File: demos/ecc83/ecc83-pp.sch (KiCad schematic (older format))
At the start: 15 parts, among them P1 IN, P2 OUT, P3 POWER, P4 CONN_2, P5 CONN_1, P6 CONN_1, P7 CONN_1, P8 CONN_1, U1 ECC83

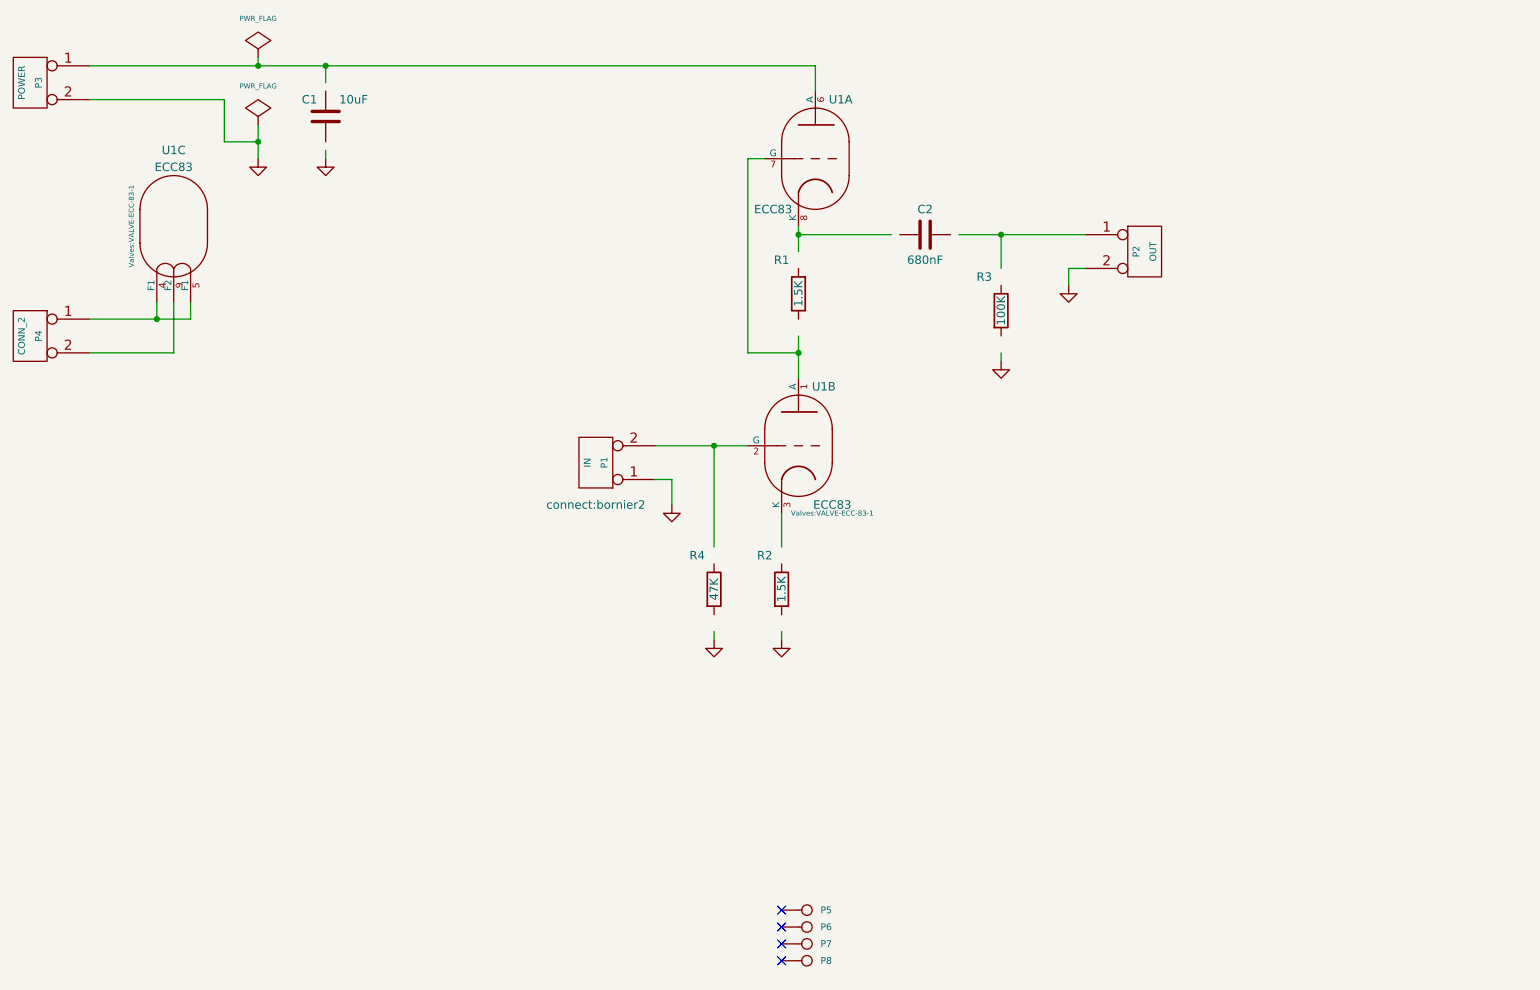
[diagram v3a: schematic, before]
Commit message: Demos: make a private library for each demo, to avoid issues when using modified kicad new schematic libraries
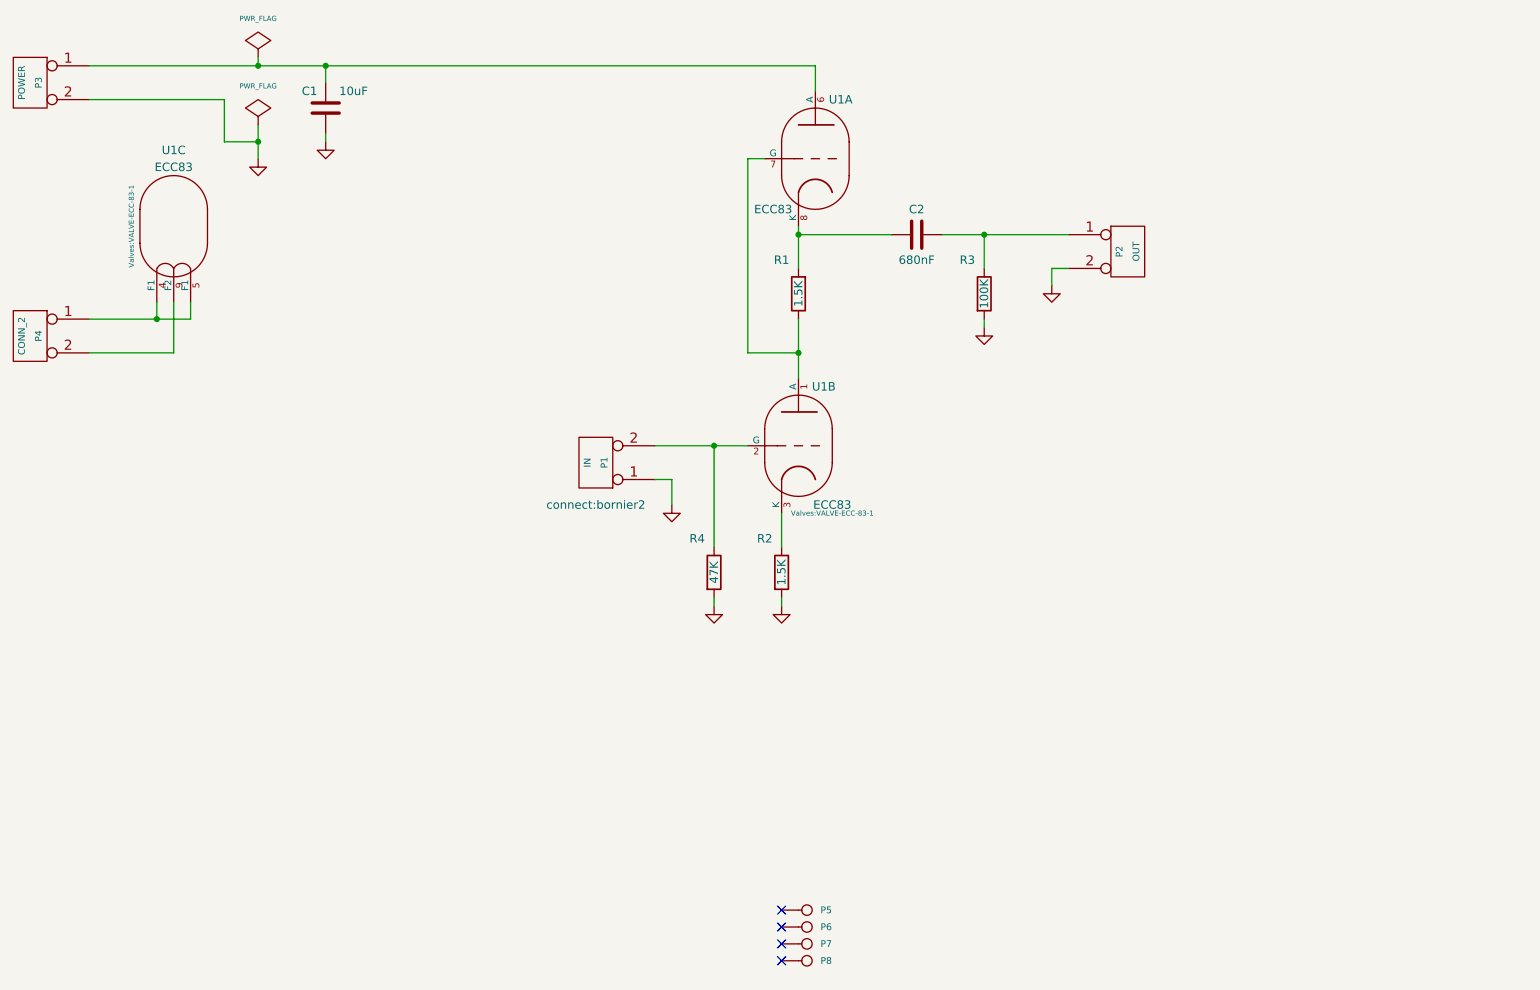
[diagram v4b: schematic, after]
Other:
- moved on the sheet: C1, C2, P2, R2, R3, R4
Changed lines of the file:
@@
 EESchema Schematic File Version 2
-LIBS:power
-LIBS:device
-LIBS:conn
-LIBS:valves
-LIBS:linear
-LIBS:regul
-LIBS:special
-LIBS:ecc83-pp-cache
+LIBS:ecc83_schlib
 EELAYER 25 0
 EELAYER END
@@
 Connection ~ 3400 2000
 Wire Wire Line
-	7150 3000 7900 3000
-Wire Wire Line
-	7400 3000 7400 3200
+	7050 3000 7800 3000
+Wire Wire Line
+	7300 3000 7300 3200
 Wire Wire Line
 	2000 3500 2600 3500
@@
 	2400 3500 2400 3400
 Wire Wire Line
-	6200 3600 6200 3850
+	6200 3500 6200 3850
 $Comp
 L ECC83 U1
@@
 L GND #PWR01
 U 1 1 457DBAF8
-P 7800 3300
-F 0 "#PWR01" H 7800 3300 30  0001 C CNN
-F 1 "GND" H 7800 3230 30  0001 C CNN
-F 2 "" H 7800 3300 60  0001 C CNN
-F 3 "" H 7800 3300 60  0001 C CNN
-	1    7800 3300
+P 7700 3300
+F 0 "#PWR01" H 7700 3300 30  0001 C CNN
+F 1 "GND" H 7700 3230 30  0001 C CNN
+F 2 "" H 7700 3300 60  0001 C CNN
+F 3 "" H 7700 3300 60  0001 C CNN
+	1    7700 3300
 	1    0    0    -1
 $EndComp
@@
 L GND #PWR02
 U 1 1 457DBAF5
-P 7400 3750
-F 0 "#PWR02" H 7400 3750 30  0001 C CNN
-F 1 "GND" H 7400 3680 30  0001 C CNN
-F 2 "" H 7400 3750 60  0001 C CNN
-F 3 "" H 7400 3750 60  0001 C CNN
-	1    7400 3750
+P 7300 3550
+F 0 "#PWR02" H 7300 3550 30  0001 C CNN
+F 1 "GND" H 7300 3480 30  0001 C CNN
+F 2 "" H 7300 3550 60  0001 C CNN
+F 3 "" H 7300 3550 60  0001 C CNN
+	1    7300 3550
 	1    0    0    -1
 $EndComp
@@
 L GND #PWR03
 U 1 1 457DBAF1
-P 6100 5400
-F 0 "#PWR03" H 6100 5400 30  0001 C CNN
-F 1 "GND" H 6100 5330 30  0001 C CNN
-F 2 "" H 6100 5400 60  0001 C CNN
-F 3 "" H 6100 5400 60  0001 C CNN
-	1    6100 5400
+P 6100 5200
+F 0 "#PWR03" H 6100 5200 30  0001 C CNN
+F 1 "GND" H 6100 5130 30  0001 C CNN
+F 2 "" H 6100 5200 60  0001 C CNN
+F 3 "" H 6100 5200 60  0001 C CNN
+	1    6100 5200
 	1    0    0    -1
 $EndComp
@@
 L GND #PWR04
 U 1 1 457DBAEF
-P 5700 5400
-F 0 "#PWR04" H 5700 5400 30  0001 C CNN
-F 1 "GND" H 5700 5330 30  0001 C CNN
-F 2 "" H 5700 5400 60  0001 C CNN
-F 3 "" H 5700 5400 60  0001 C CNN
-	1    5700 5400
+P 5700 5200
+F 0 "#PWR04" H 5700 5200 30  0001 C CNN
+F 1 "GND" H 5700 5130 30  0001 C CNN
+F 2 "" H 5700 5200 60  0001 C CNN
+F 3 "" H 5700 5200 60  0001 C CNN
+	1    5700 5200
 	1    0    0    -1
 $EndComp
@@
 L C C1
 U 1 1 4549F4BE
-P 3400 2300
-F 0 "C1" H 3450 2400 50  0000 L CNN
-F 1 "10uF" H 3150 2400 50  0000 L CNN
-F 2 "discret:C2V10" H 3400 2300 60  0001 C CNN
-F 3 "" H 3400 2300 60  0001 C CNN
-	1    3400 2300
+P 3400 2250
+F 0 "C1" H 3450 2350 50  0000 L CNN
+F 1 "10uF" H 3150 2350 50  0000 L CNN
+F 2 "discret:C2V10" H 3400 2250 60  0001 C CNN
+F 3 "" H 3400 2250 60  0001 C CNN
+	1    3400 2250
 	-1   0    0    -1
 $EndComp
@@
 L CONN_2 P2
 U 1 1 4549F46C
-P 8250 3100
-F 0 "P2" V 8200 3100 40  0000 C CNN
-F 1 "OUT" V 8300 3100 40  0000 C CNN
-F 2 "connect:bornier2" H 8250 3100 60  0001 C CNN
-F 3 "" H 8250 3100 60  0001 C CNN
-	1    8250 3100
+P 8150 3100
+F 0 "P2" V 8100 3100 40  0000 C CNN
+F 1 "OUT" V 8200 3100 40  0000 C CNN
+F 2 "connect:bornier2" H 8150 3100 60  0001 C CNN
+F 3 "" H 8150 3100 60  0001 C CNN
+	1    8150 3100
 	1    0    0    -1
 $EndComp
@@
 L C C2
 U 1 1 4549F3BE
-P 6950 3000
-F 0 "C2" V 6800 3000 50  0000 C CNN
-F 1 "680nF" V 7100 3000 50  0000 C CNN
-F 2 "discret:C2" H 6950 3000 60  0001 C CNN
-F 3 "" H 6950 3000 60  0001 C CNN
-	1    6950 3000
+P 6900 3000
+F 0 "C2" V 6750 3000 50  0000 C CNN
+F 1 "680nF" V 7050 3000 50  0000 C CNN
+F 2 "discret:C2" H 6900 3000 60  0001 C CNN
+F 3 "" H 6900 3000 60  0001 C CNN
+	1    6900 3000
 	0    1    1    0
 $EndComp
@@
 L R R3
 U 1 1 4549F3AD
-P 7400 3450
-F 0 "R3" H 7300 3650 50  0000 C CNN
-F 1 "100K" V 7400 3450 50  0000 C CNN
-F 2 "discret:R3" H 7400 3450 60  0001 C CNN
-F 3 "" H 7400 3450 60  0001 C CNN
-	1    7400 3450
+P 7300 3350
+F 0 "R3" H 7200 3550 50  0000 C CNN
+F 1 "100K" V 7300 3350 50  0000 C CNN
+F 2 "discret:R3" H 7300 3350 60  0001 C CNN
+F 3 "" H 7300 3350 60  0001 C CNN
+	1    7300 3350
 	1    0    0    -1
 $EndComp
@@
 L R R4
 U 1 1 4549F3A2
-P 5700 5100
-F 0 "R4" H 5600 5300 50  0000 C CNN
-F 1 "47K" V 5700 5100 50  0000 C CNN
-F 2 "discret:R3" H 5700 5100 60  0001 C CNN
-F 3 "" H 5700 5100 60  0001 C CNN
-	1    5700 5100
+P 5700 5000
+F 0 "R4" H 5600 5200 50  0000 C CNN
+F 1 "47K" V 5700 5000 50  0000 C CNN
+F 2 "discret:R3" H 5700 5000 60  0001 C CNN
+F 3 "" H 5700 5000 60  0001 C CNN
+	1    5700 5000
 	1    0    0    -1
 $EndComp
@@
 L R R2
 U 1 1 4549F39D
-P 6100 5100
-F 0 "R2" H 6000 5300 50  0000 C CNN
-F 1 "1.5K" V 6100 5100 50  0000 C CNN
-F 2 "discret:R3" H 6100 5100 60  0001 C CNN
-F 3 "" H 6100 5100 60  0001 C CNN
-	1    6100 5100
+P 6100 5000
+F 0 "R2" H 6000 5200 50  0000 C CNN
+F 1 "1.5K" V 6100 5000 50  0000 C CNN
+F 2 "discret:R3" H 6100 5000 60  0001 C CNN
+F 3 "" H 6100 5000 60  0001 C CNN
+	1    6100 5000
 	1    0    0    -1
 $EndComp
@@
 L GND #PWR06
 U 1 1 53B6F370
-P 3400 2550
-F 0 "#PWR06" H 3400 2550 30  0001 C CNN
-F 1 "GND" H 3400 2480 30  0001 C CNN
-F 2 "" H 3400 2550 60  0001 C CNN
-F 3 "" H 3400 2550 60  0001 C CNN
-	1    3400 2550
+P 3400 2450
+F 0 "#PWR06" H 3400 2450 30  0001 C CNN
+F 1 "GND" H 3400 2380 30  0001 C CNN
+F 2 "" H 3400 2450 60  0001 C CNN
+F 3 "" H 3400 2450 60  0001 C CNN
+	1    3400 2450
 	-1   0    0    -1
 $EndComp
@@
 Connection ~ 5700 4250
 Wire Wire Line
-	6200 2950 6200 3100
+	6200 2950 6200 3200
 Connection ~ 6200 3700
 Wire Wire Line
@@
 Wire Wire Line
 	5900 3700 6200 3700
-Connection ~ 7400 3000
+Connection ~ 7300 3000
 Wire Wire Line
 	6750 3000 6200 3000
@@
 	3400 2100 3400 2000
 Wire Wire Line
-	3400 2550 3400 2500
+	3400 2450 3400 2400
 $Comp
 L PWR_FLAG #FLG07
@@
 	5450 4450 5350 4450
 Wire Wire Line
-	6100 5350 6100 5400
-Wire Wire Line
-	5700 5350 5700 5400
-Wire Wire Line
-	7900 3200 7800 3200
-Wire Wire Line
-	7800 3200 7800 3300
-Wire Wire Line
-	7400 3750 7400 3700
+	6100 5150 6100 5200
+Wire Wire Line
+	5700 5150 5700 5200
+Wire Wire Line
+	7800 3200 7700 3200
+Wire Wire Line
+	7700 3200 7700 3300
+Wire Wire Line
+	7300 3550 7300 3500
 NoConn ~ 6100 7000
 NoConn ~ 6100 7100
